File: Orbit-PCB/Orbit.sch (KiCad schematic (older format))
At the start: 294 parts, among them J1 PJ-3200B-4A, J10 Breakaway_Tabs, J11 PJ-3200B-4A, J12 AVR-ISP-6, J13 Breakaway_Tabs, J14 Breakaway_Tabs, J17 Breakaway_Tabs, J18 Breakaway_Tabs, J19 Breakaway_Tabs, J2 AVR-ISP-6, J20 Breakaway_Tabs, J3 Breakaway_Tabs, J5 Breakaway_Tabs, J6 Breakaway_Tabs, J7 Breakaway_Tabs, J9 Breakaway_Tabs, Q1 2N7002, Q2 2N7002, SW1 SW_Push, SW2 SW_Push, U1 ATmega32U4-MU, U2 PRTR5V0U2X, U3 ATmega32U4-MU, U4 PRTR5V0U2X, Y1 16MHz, Y2 16MHz

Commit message: Finish routing
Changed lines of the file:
@@
 	3600 1000 3600 1050
 Connection ~ 3600 1050
+Wire Wire Line
+	3400 1000 3400 1050
+Wire Wire Line
+	2625 2150 2900 2150
 $Comp
-L power:VCC #PWR?
-U 1 1 5C476C25
+L power:VBUS #PWR?
+U 1 1 5BF23610
 P 3400 1000
 F 0 "#PWR?" H 3400 850 50  0001 C CNN
-F 1 "VCC" H 3417 1173 50  0000 C CNN
+F 1 "VBUS" H 3415 1173 50  0000 C CNN
 F 2 "" H 3400 1000 50  0001 C CNN
 F 3 "" H 3400 1000 50  0001 C CNN
@@
 	1    0    0    -1
 $EndComp
-Wire Wire Line
-	3400 1000 3400 1050
 $Comp
-L power:VCC #PWR?
-U 1 1 5C4F4A47
+L power:VBUS #PWR?
+U 1 1 5BF2387E
 P 2625 2150
 F 0 "#PWR?" H 2625 2000 50  0001 C CNN
-F 1 "VCC" H 2642 2323 50  0000 C CNN
+F 1 "VBUS" H 2640 2323 50  0000 C CNN
 F 2 "" H 2625 2150 50  0001 C CNN
 F 3 "" H 2625 2150 50  0001 C CNN
@@
 	1    0    0    -1
 $EndComp
-Wire Wire Line
-	2625 2150 2900 2150
 $EndSCHEMATC

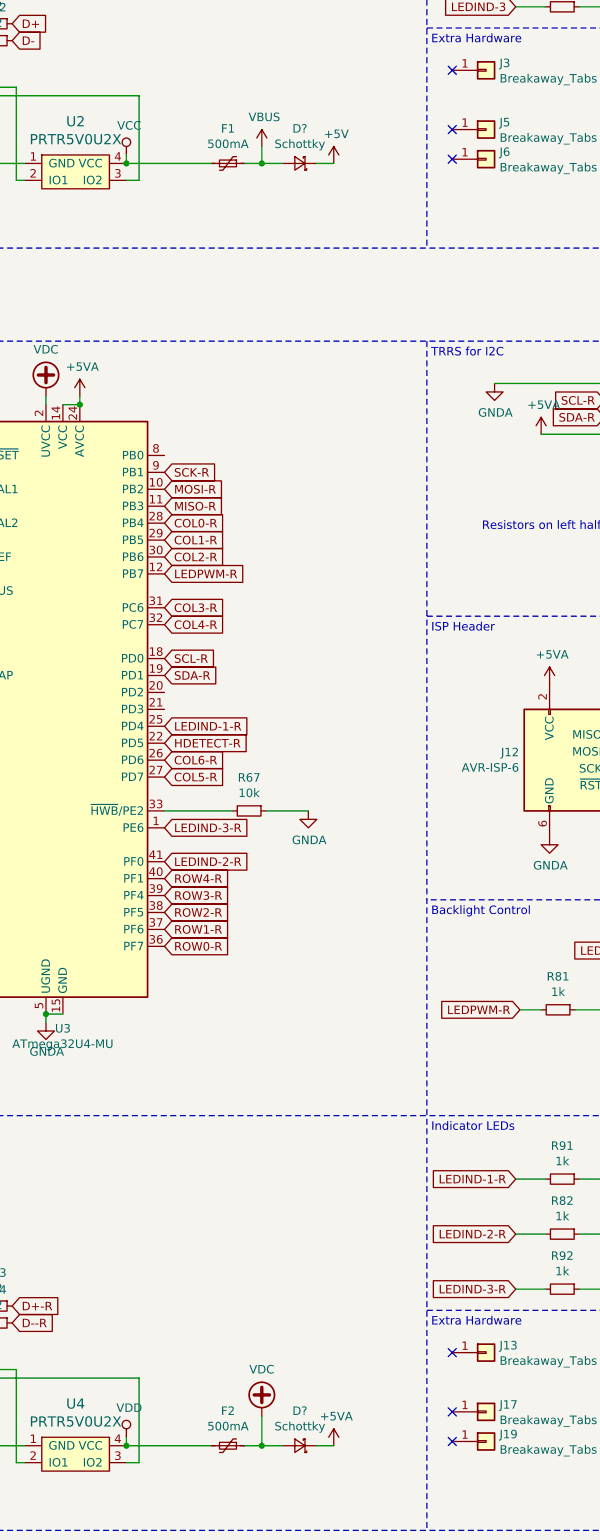
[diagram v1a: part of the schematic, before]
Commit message: Generate new BOM
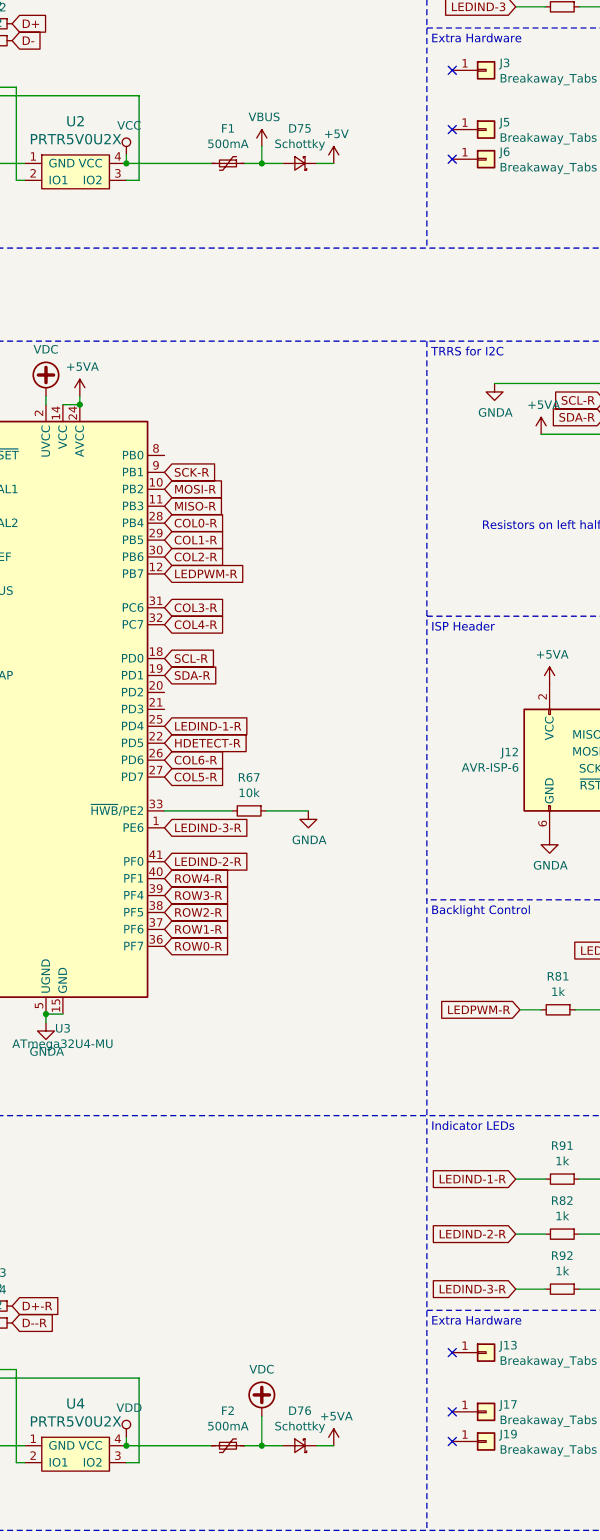
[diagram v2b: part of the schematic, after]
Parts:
- gave numbers to parts that had none: 2
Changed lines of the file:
@@
 	2325 8925 2900 8925
 $Comp
-L Device:D_Schottky_Small D?
+L Device:D_Schottky_Small D75
 U 1 1 5BF8426A
 P 4900 7200
-F 0 "D?" H 4900 6995 50  0000 C CNN
+F 0 "D75" H 4900 6995 50  0000 C CNN
 F 1 "Schottky" H 4900 7086 50  0000 C CNN
 F 2 "Diodes_SMD:D_SOD-123" V 4900 7200 50  0001 C CNN
@@
 	5100 7200 5000 7200
 $Comp
-L power:VBUS #PWR?
+L power:VBUS #PWR0104
 U 1 1 5C001278
 P 4675 7100
-F 0 "#PWR?" H 4675 6950 50  0001 C CNN
+F 0 "#PWR0104" H 4675 6950 50  0001 C CNN
 F 1 "VBUS" H 4690 7273 50  0000 C CNN
 F 2 "" H 4675 7100 50  0001 C CNN
@@
 	4675 7200 4575 7200
 $Comp
-L Device:D_Schottky_Small D?
+L Device:D_Schottky_Small D76
 U 1 1 5C07FDD0
 P 4900 14775
-F 0 "D?" H 4900 14570 50  0000 C CNN
+F 0 "D76" H 4900 14570 50  0000 C CNN
 F 1 "Schottky" H 4900 14661 50  0000 C CNN
 F 2 "Diodes_SMD:D_SOD-123" V 4900 14775 50  0001 C CNN
@@
 	5100 14775 5000 14775
 $Comp
-L power:VDC #PWR?
+L power:VDC #PWR0107
 U 1 1 5C1030A0
 P 4675 14600
-F 0 "#PWR?" H 4675 14500 50  0001 C CNN
+F 0 "#PWR0107" H 4675 14500 50  0001 C CNN
 F 1 "VDC" H 4675 14875 50  0000 C CNN
 F 2 "" H 4675 14600 50  0001 C CNN
@@
 Connection ~ 3600 8625
 $Comp
-L power:VDC #PWR?
+L power:VDC #PWR0138
 U 1 1 5C2FA9D3
 P 3400 8575
-F 0 "#PWR?" H 3400 8475 50  0001 C CNN
+F 0 "#PWR0138" H 3400 8475 50  0001 C CNN
 F 1 "VDC" H 3400 8850 50  0000 C CNN
 F 2 "" H 3400 8575 50  0001 C CNN
@@
 	3400 8575 3400 8625
 $Comp
-L power:VDC #PWR?
+L power:VDC #PWR0143
 U 1 1 5C378C46
 P 2625 9725
-F 0 "#PWR?" H 2625 9625 50  0001 C CNN
+F 0 "#PWR0143" H 2625 9625 50  0001 C CNN
 F 1 "VDC" H 2625 10000 50  0000 C CNN
 F 2 "" H 2625 9725 50  0001 C CNN
@@
 	2625 2150 2900 2150
 $Comp
-L power:VBUS #PWR?
+L power:VBUS #PWR0147
 U 1 1 5BF23610
 P 3400 1000
-F 0 "#PWR?" H 3400 850 50  0001 C CNN
+F 0 "#PWR0147" H 3400 850 50  0001 C CNN
 F 1 "VBUS" H 3415 1173 50  0000 C CNN
 F 2 "" H 3400 1000 50  0001 C CNN
@@
 $EndComp
 $Comp
-L power:VBUS #PWR?
+L power:VBUS #PWR0148
 U 1 1 5BF2387E
 P 2625 2150
-F 0 "#PWR?" H 2625 2000 50  0001 C CNN
+F 0 "#PWR0148" H 2625 2000 50  0001 C CNN
 F 1 "VBUS" H 2640 2323 50  0000 C CNN
 F 2 "" H 2625 2150 50  0001 C CNN

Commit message: Add a comment
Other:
- note added: "RIGHT HAND SCHEMATIC\n\nPower net changes:\nVCC -> VDD\nVBUS -> VDC\nGND -> GNDA\n+5V -> +5VA\nto prevent kicad from complaining about no connections between halves"
- note removed: "RIGHT HAND SCHEMATIC\n\nPower net changes:\nVCC -> VDD\nGND -> GNDA\n+5V -> +5VA\nto prevent kicad from complaining about no connections between halves"
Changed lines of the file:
@@
 LEFT HAND SCHEMATIC
 Text Notes 11100 15225 0    50   ~ 10
-RIGHT HAND SCHEMATIC\n\nPower net changes:\nVCC -> VDD\nGND -> GNDA\n+5V -> +5VA\nto prevent kicad from complaining about no connections between halves
+RIGHT HAND SCHEMATIC\n\nPower net changes:\nVCC -> VDD\nVBUS -> VDC\nGND -> GNDA\n+5V -> +5VA\nto prevent kicad from complaining about no connections between halves
 $Comp
 L power:VDD #PWR0123

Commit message: Generate 2.1 production data
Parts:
- Y1, Y2: footprint Crystals:Crystal_SMD_2520-4pin_2.5x2.0mm -> Crystals:Crystal_SMD_3225-4pin_3.2x2.5mm
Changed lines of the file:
@@
 F 0 "Y1" V 2479 1816 50  0000 L CNN
 F 1 "16MHz" V 2570 1816 50  0000 L CNN
-F 2 "Crystals:Crystal_SMD_2520-4pin_2.5x2.0mm" H 2525 1650 50  0001 C CNN
+F 2 "Crystals:Crystal_SMD_3225-4pin_3.2x2.5mm" H 2525 1650 50  0001 C CNN
 F 3 "~" H 2525 1650 50  0001 C CNN
 	1    2525 1650
@@
 F 0 "Y2" V 2479 9391 50  0000 L CNN
 F 1 "16MHz" V 2570 9391 50  0000 L CNN
-F 2 "Crystals:Crystal_SMD_2520-4pin_2.5x2.0mm" H 2525 9225 50  0001 C CNN
+F 2 "Crystals:Crystal_SMD_3225-4pin_3.2x2.5mm" H 2525 9225 50  0001 C CNN
 F 3 "~" H 2525 9225 50  0001 C CNN
 	1    2525 9225

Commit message: Update PCB to V2.2 - Differing pinout on each half
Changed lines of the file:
@@
 Text Notes 5675 5350 0    50   ~ 0
 Indicator LEDs\n
-Text GLabel 4100 1750 2    50   Input ~ 0
+Text GLabel 4100 2350 2    50   Input ~ 0
 COL0
-Text GLabel 4100 1850 2    50   Input ~ 0
+Text GLabel 4100 1750 2    50   Input ~ 0
 COL1
-Text GLabel 4100 1950 2    50   Input ~ 0
+Text GLabel 4100 3250 2    50   Input ~ 0
 COL2
-Text GLabel 4100 2250 2    50   Input ~ 0
+Text GLabel 4100 3150 2    50   Input ~ 0
 COL3
-Text GLabel 4100 2350 2    50   Input ~ 0
+Text GLabel 4100 2950 2    50   Input ~ 0
 COL4
-Text GLabel 4100 3250 2    50   Input ~ 0
+Text GLabel 4100 3850 2    50   Input ~ 0
 COL5
 Connection ~ 2900 1350
@@
 Wire Wire Line
 	4500 3450 4100 3450
-Text GLabel 4100 3150 2    50   Input ~ 0
+Text GLabel 4100 3750 2    50   Input ~ 0
 COL6
 Text GLabel 4100 4250 2    50   Input ~ 0
@@
 Text GLabel 4100 3950 2    50   Input ~ 0
 ROW3
-Text GLabel 4100 3850 2    50   Input ~ 0
+Text GLabel 4100 2850 2    50   Input ~ 0
 ROW4
-Text GLabel 4100 2950 2    50   Input ~ 0
+Text GLabel 4100 1850 2    50   Input ~ 0
 LEDIND-1
 Wire Notes Line
@@
 Text Notes 5675 12925 0    50   ~ 0
 Indicator LEDs\n
-Text GLabel 4100 9325 2    50   Input ~ 0
+Text GLabel 4100 10525 2    50   Input ~ 0
 COL0-R
-Text GLabel 4100 9425 2    50   Input ~ 0
+Text GLabel 4100 10725 2    50   Input ~ 0
 COL1-R
-Text GLabel 4100 9525 2    50   Input ~ 0
+Text GLabel 4100 11425 2    50   Input ~ 0
 COL2-R
-Text GLabel 4100 9825 2    50   Input ~ 0
+Text GLabel 4100 11325 2    50   Input ~ 0
 COL3-R
-Text GLabel 4100 9925 2    50   Input ~ 0
+Text GLabel 4100 11525 2    50   Input ~ 0
 COL4-R
-Text GLabel 4100 10825 2    50   Input ~ 0
+Text GLabel 4100 11625 2    50   Input ~ 0
 COL5-R
 Connection ~ 2900 8925
@@
 Wire Wire Line
 	4500 11025 4100 11025
-Text GLabel 4100 10725 2    50   Input ~ 0
+Text GLabel 4100 9825 2    50   Input ~ 0
 COL6-R
-Text GLabel 4100 11825 2    50   Input ~ 0
+Text GLabel 4100 9525 2    50   Input ~ 0
 ROW0-R
-Text GLabel 4100 11725 2    50   Input ~ 0
+Text GLabel 4100 9425 2    50   Input ~ 0
 ROW1-R
-Text GLabel 4100 11625 2    50   Input ~ 0
+Text GLabel 4100 9325 2    50   Input ~ 0
 ROW2-R
-Text GLabel 4100 11525 2    50   Input ~ 0
+Text GLabel 4100 10825 2    50   Input ~ 0
 ROW3-R
-Text GLabel 4100 11425 2    50   Input ~ 0
+Text GLabel 4100 11125 2    50   Input ~ 0
 ROW4-R
-Text GLabel 4100 10525 2    50   Input ~ 0
+Text GLabel 4100 11725 2    50   Input ~ 0
 LEDIND-1-R
 Wire Notes Line
@@
 Wire Wire Line
 	7250 13850 7250 13525
-Text GLabel 4100 3750 2    50   Input ~ 0
+Text GLabel 4100 1950 2    50   Input ~ 0
 LEDIND-2
-Text GLabel 4100 3550 2    50   Input ~ 0
+Text GLabel 4100 2250 2    50   Input ~ 0
 LEDIND-3
-Text GLabel 4100 11325 2    50   Input ~ 0
+Text GLabel 4100 11825 2    50   Input ~ 0
 LEDIND-2-R
-Text GLabel 4100 11125 2    50   Input ~ 0
+Text GLabel 4100 9925 2    50   Input ~ 0
 LEDIND-3-R
 Wire Notes Line
